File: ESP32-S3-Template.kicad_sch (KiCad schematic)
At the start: 3 parts, among them J2 Conn_01x22, J3 Conn_01x22

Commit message: a little bit of a reorg
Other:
- note added: "PSRAM"
- note removed: "OCTAL"
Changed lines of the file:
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@@
 		)
 	)
-	(text "OCTAL"
+	(text "PSRAM"
 		(exclude_from_sim no)
 		(at 113.792 125.73 90)
@@
 		(at 166.37 190.5 0)
 		(unit 1)
-		(exclude_from_sim no)
+		(exclude_from_sim yes)
 		(in_bom no)
 		(on_board yes)
@@
 		)
 		(property "Description" "Open Hardware logo, small"
-			(at 166.37 190.5 0)
-			(effects
-				(font
-					(size 1.27 1.27)
-				)
-				(hide yes)
-			)
-		)
-		(property "Sim.Enable" "0"
 			(at 166.37 190.5 0)
 			(effects
@@
 		)
 		(instances
-			(project "ESP32-S3-Breakout"
+			(project "ESP32-S3-Template"
 				(path "/3bba1511-25ec-43a9-bde1-3bab06c08341"
 					(page "2")

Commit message: checking bom
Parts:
- J2, J3: now left out of the parts list
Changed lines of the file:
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@@
 		(unit 1)
 		(exclude_from_sim no)
-		(in_bom yes)
+		(in_bom no)
 		(on_board yes)
 		(dnp no)
@@
 		(unit 1)
 		(exclude_from_sim no)
-		(in_bom yes)
-		(on_board yes)
-		(dnp no)
+		(in_bom no)
+		(on_board yes)
+		(dnp no)

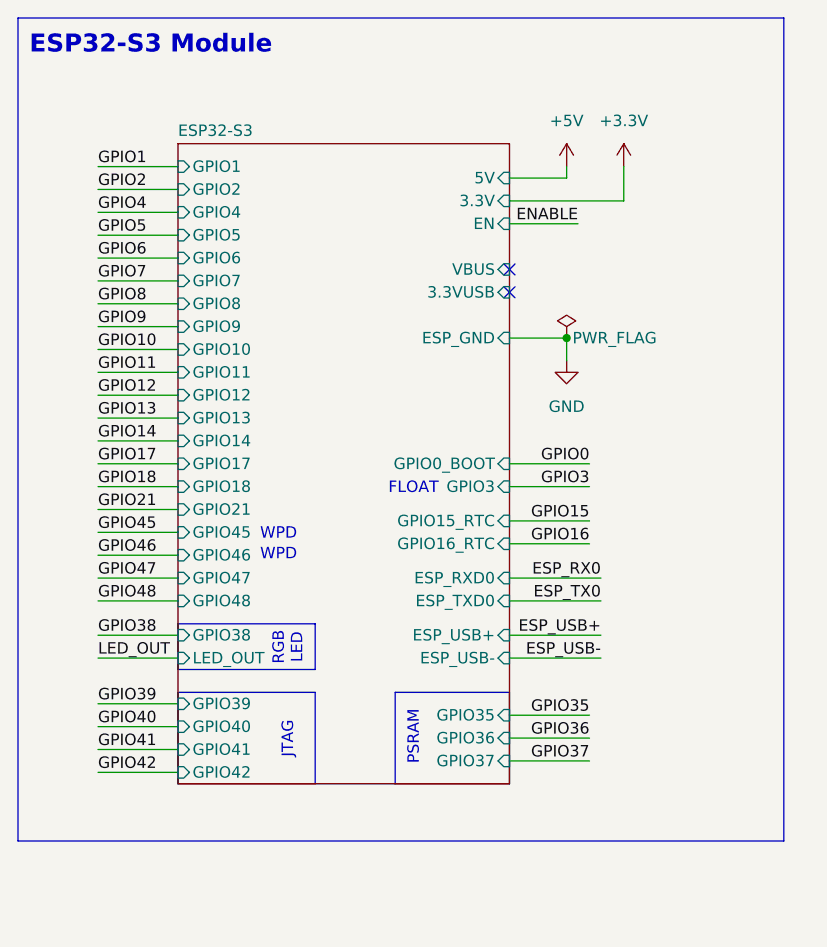
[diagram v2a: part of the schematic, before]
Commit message: reworked the esp module symbol with more pin info.
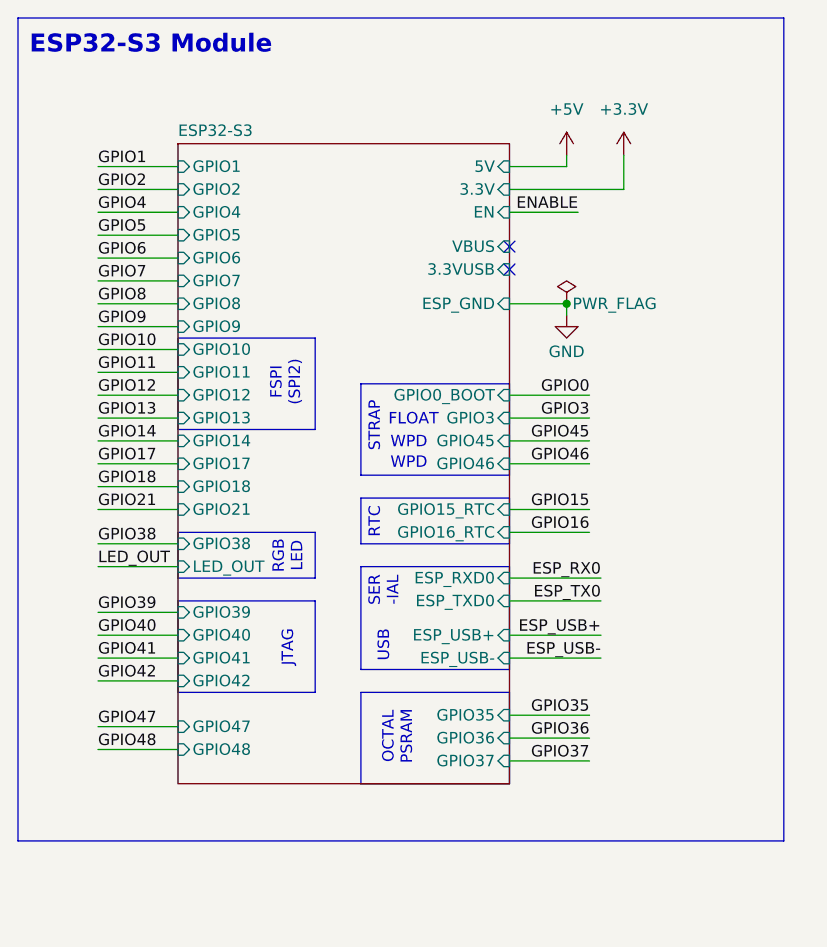
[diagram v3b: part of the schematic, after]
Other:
- note added: "FSPI (SPI2)"
- note added: "OCTAL PSRAM"
- note added: "RTC"
- note added: "SER -IAL"
- note added: "STRAP"
- note added: "USB"
- note removed: "PSRAM"

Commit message: another full pass over the schematic and layout
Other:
- title: (none) -> https://github.com/hoeken/ESP32-S3-Template
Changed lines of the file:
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@@
 	(generator_version "9.0")
 	(paper "A4")
+	(title_block
+		(title "https://github.com/hoeken/ESP32-S3-Template")
+		(date "2025-08-28")
+		(rev "A")
+	)
 	(rectangle
 		(start 107.95 120.65)

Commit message: pulled in brineomatic version
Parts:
- renumbered J2 to J1, J3 to J2
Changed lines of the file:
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@@
 		(dnp no)
 		(fields_autoplaced yes)
-		(property "Reference" "#PWR013"
+		(property "Reference" "#PWR06"
 			(at 179.07 67.31 0)
 			(effects
@@
 			(project "ESP32-S3-Breakout"
 				(path "/3bba1511-25ec-43a9-bde1-3bab06c08341"
-					(reference "#PWR013")
+					(reference "#PWR06")
 					(unit 1)
 				)
@@
 		(dnp no)
 		(fields_autoplaced yes)
-		(property "Reference" "J2"
+		(property "Reference" "J1"
 			(at 194.31 91.4399 0)
 			(effects
@@
 			(project ""
 				(path "/3bba1511-25ec-43a9-bde1-3bab06c08341"
-					(reference "J2")
+					(reference "J1")
 					(unit 1)
 				)
@@
 		(on_board yes)
 		(dnp no)
-		(property "Reference" "#PWR022"
+		(property "Reference" "#PWR07"
 			(at 232.41 128.27 0)
 			(effects
@@
 			(project "ESP32-S3-Breakout"
 				(path "/3bba1511-25ec-43a9-bde1-3bab06c08341"
-					(reference "#PWR022")
+					(reference "#PWR07")
 					(unit 1)
 				)
@@
 		(dnp no)
 		(fields_autoplaced yes)
-		(property "Reference" "#PWR020"
+		(property "Reference" "#PWR04"
 			(at 173.99 118.11 0)
 			(effects
@@
 			(project "ESP32-S3-Breakout"
 				(path "/3bba1511-25ec-43a9-bde1-3bab06c08341"
-					(reference "#PWR020")
+					(reference "#PWR04")
 					(unit 1)
 				)
@@
 		(on_board yes)
 		(dnp no)
-		(property "Reference" "#PWR021"
+		(property "Reference" "#PWR05"
 			(at 173.99 128.27 0)
 			(effects
@@
 			(project "ESP32-S3-Breakout"
 				(path "/3bba1511-25ec-43a9-bde1-3bab06c08341"
-					(reference "#PWR021")
+					(reference "#PWR05")
 					(unit 1)
 				)
@@
 		(on_board yes)
 		(dnp no)
-		(property "Reference" "#PWR023"
+		(property "Reference" "#PWR08"
 			(at 233.68 74.93 0)
 			(effects
@@
 			(project "ESP32-S3-Breakout"
 				(path "/3bba1511-25ec-43a9-bde1-3bab06c08341"
-					(reference "#PWR023")
+					(reference "#PWR08")
 					(unit 1)
 				)
@@
 		(dnp no)
 		(fields_autoplaced yes)
-		(property "Reference" "#PWR02"
+		(property "Reference" "#PWR01"
 			(at 130.81 64.77 0)
 			(effects
@@
 			(project ""
 				(path "/3bba1511-25ec-43a9-bde1-3bab06c08341"
-					(reference "#PWR02")
+					(reference "#PWR01")
 					(unit 1)
 				)
@@
 		(on_board yes)
 		(dnp no)
-		(property "Reference" "#PWR01"
+		(property "Reference" "#PWR02"
 			(at 130.81 85.09 0)
 			(effects
@@
 			(project ""
 				(path "/3bba1511-25ec-43a9-bde1-3bab06c08341"
-					(reference "#PWR01")
+					(reference "#PWR02")
 					(unit 1)
 				)
@@
 		(on_board yes)
 		(dnp no)
-		(property "Reference" "J3"
+		(property "Reference" "J2"
 			(at 212.09 91.4399 0)
 			(effects
@@
 			(project "ESP32-S3-Breakout"
 				(path "/3bba1511-25ec-43a9-bde1-3bab06c08341"
-					(reference "J3")
-					(unit 1)
-				)
+					(reference "J2")
+					(unit 1)
+				)
